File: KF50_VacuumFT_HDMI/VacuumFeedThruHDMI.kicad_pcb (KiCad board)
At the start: 4 copper layers, 142 x 154 mm, 16 parts, among them J1 DB25_Male, J1_(1:4) HDMI_A_1.4, J1_(5:8) HDMI_A_1.4, J1_(9:12) HDMI_A_1.4, J2 Conn_01x08, J2 DB25_Male, J2_(1:4) HDMI_A_1.4, J2_(5:8) HDMI_A_1.4, J2_(9:12) HDMI_A_1.4, J3 DB25_Male, J3_(1:4) HDMI_A_1.4, J3_(5:8) HDMI_A_1.4, J3_(9:12) HDMI_A_1.4

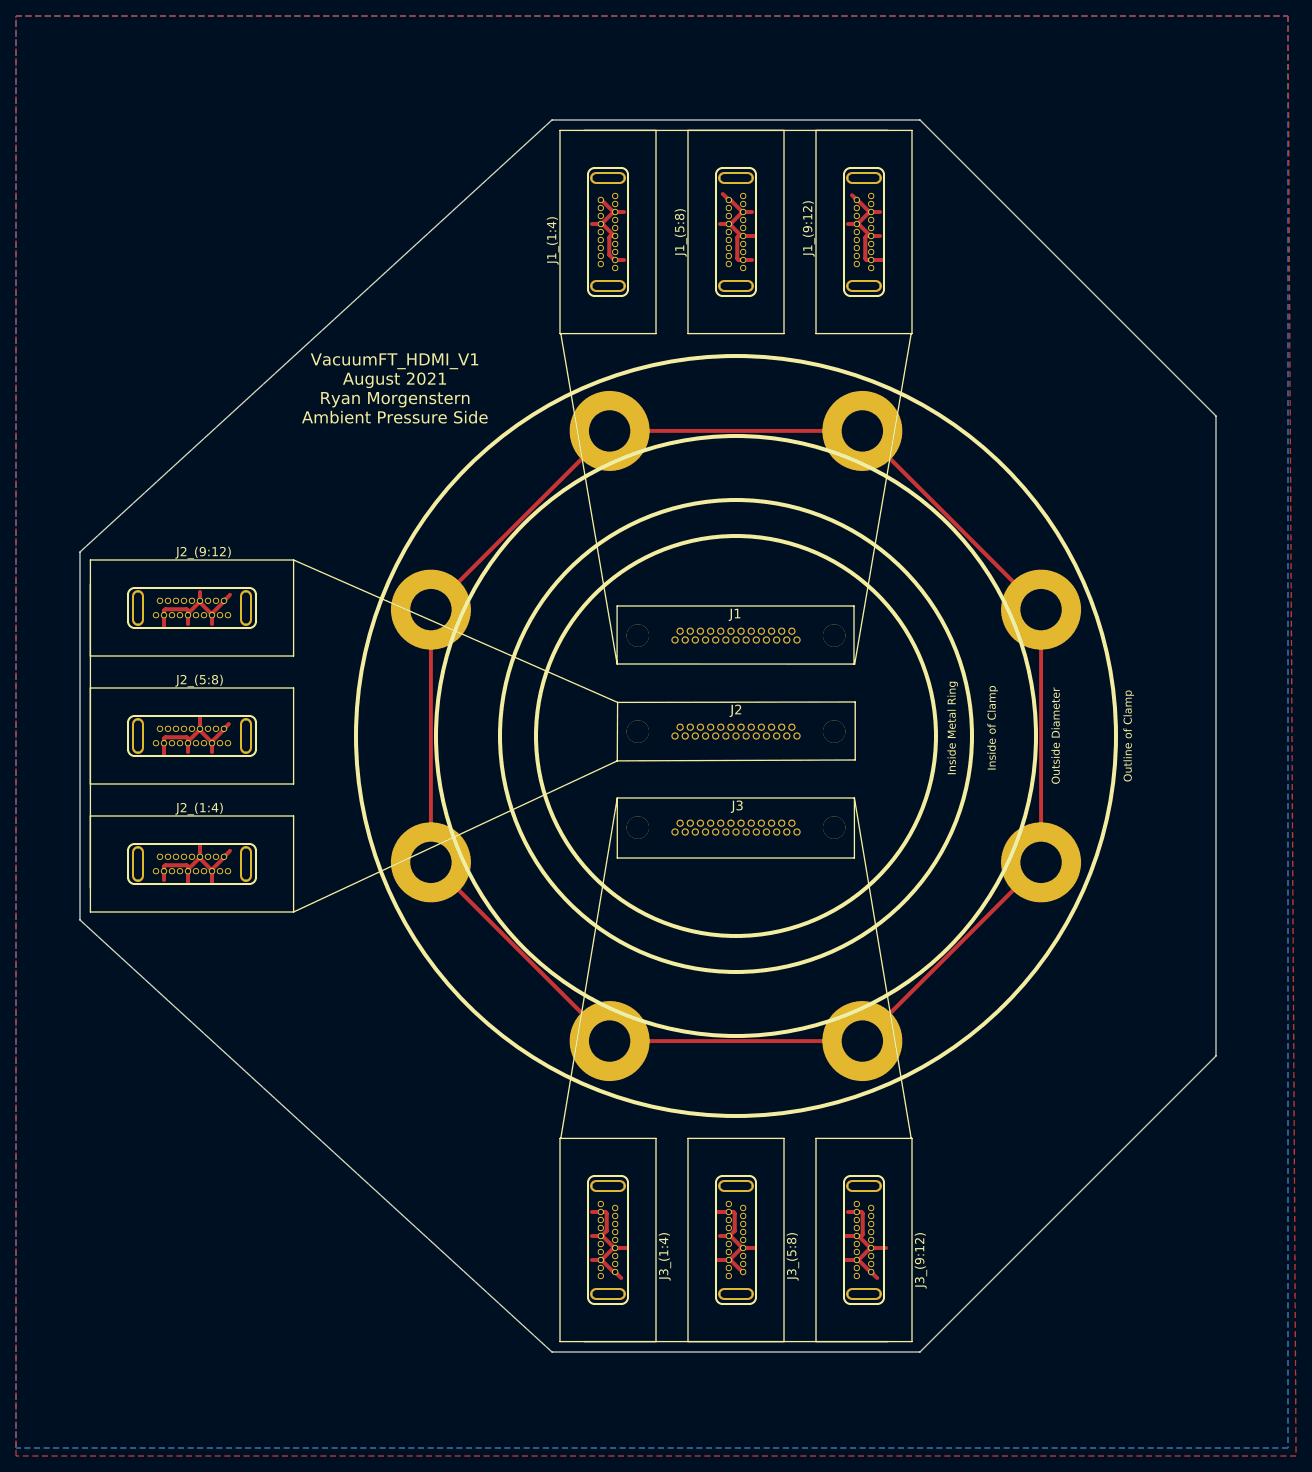
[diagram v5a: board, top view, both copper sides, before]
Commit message: Update Annotations and Surface Mounts
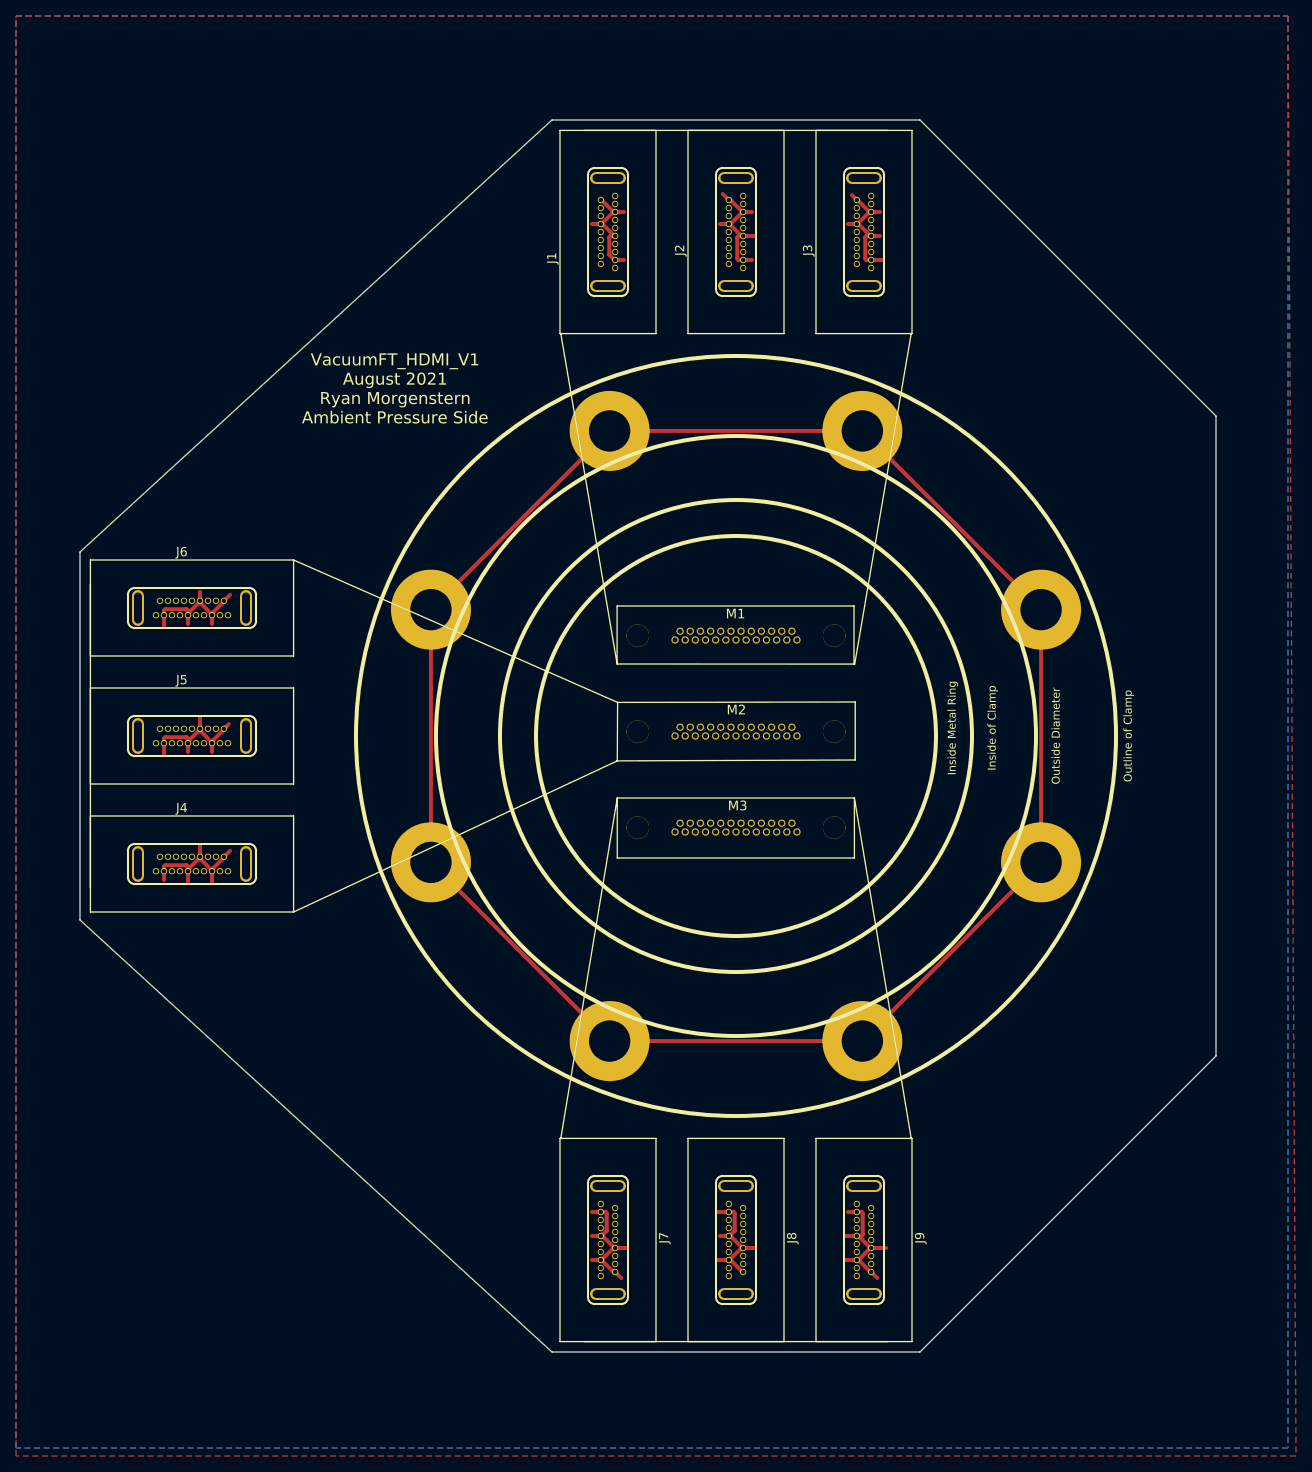
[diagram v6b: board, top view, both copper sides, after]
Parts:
- renumbered J1_(1:4) to J1, J1_(5:8) to J2, J1_(9:12) to J3, J2_(1:4) to J4, J2_(5:8) to J5, J2_(9:12) to J6, J3_(1:4) to J7, J3_(5:8) to J8, J3_(9:12) to J9, J1 to M1, J2 to M2, J3 to M3
